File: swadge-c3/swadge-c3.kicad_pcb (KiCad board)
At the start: 2 copper layers, 73.7 x 89.4 mm, 73 parts, among them J1 USB_B_Micro, M1 Motor_DC, Q1 Q_NPN_BEC, SW0 4-1437565-2, SW1 4-1437565-2, SW2 4-1437565-2, SW3 4-1437565-2, SW4 LEVER8184, SW5 SW_SPDT, U1 GS321-TR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

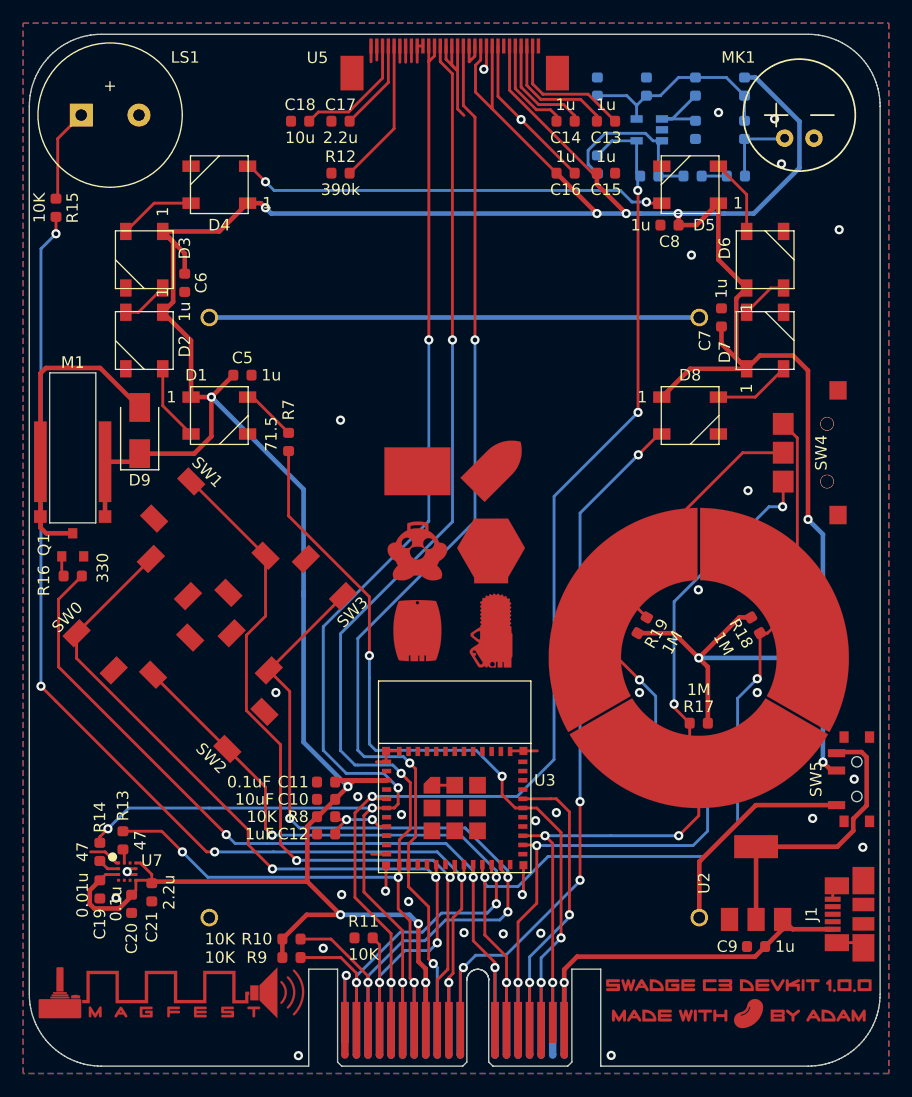
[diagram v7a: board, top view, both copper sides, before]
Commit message: Move around resistors, silk
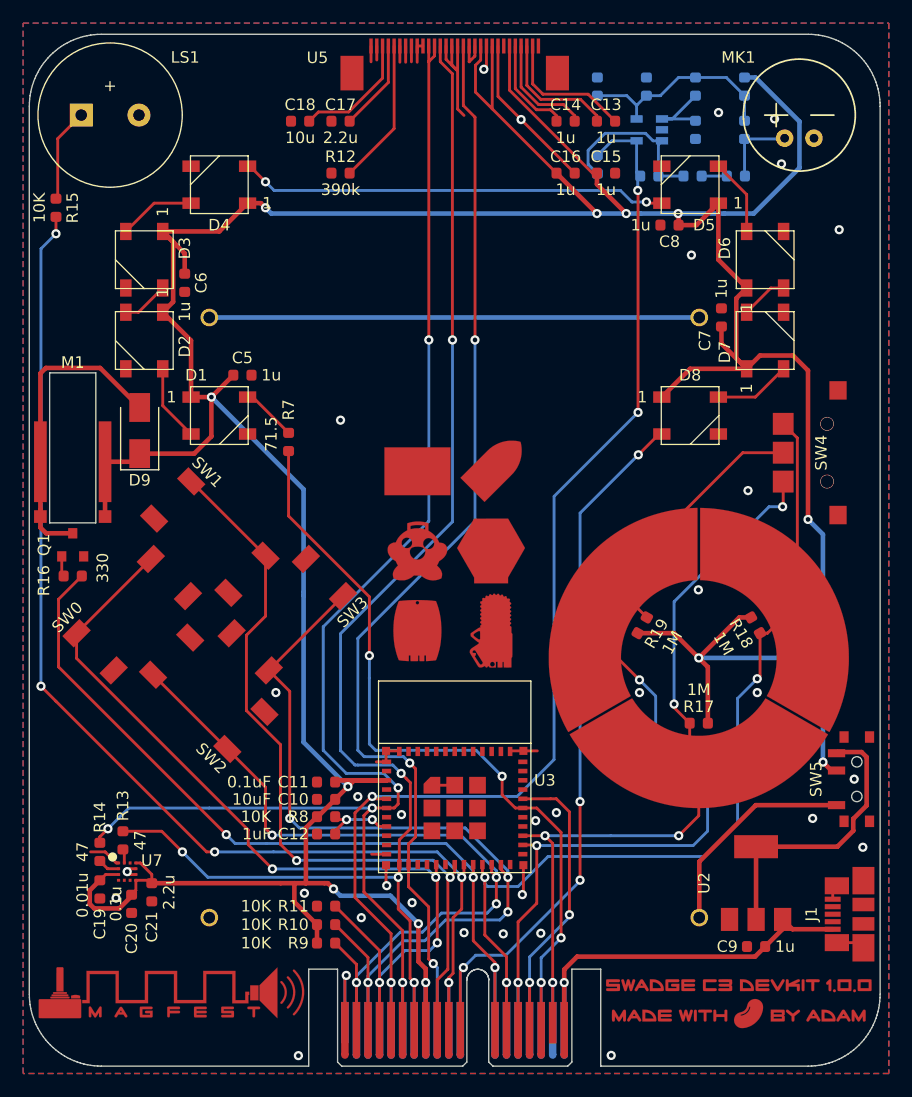
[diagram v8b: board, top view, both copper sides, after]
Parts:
- moved R11 4.26 mm to (134.2, 133.5)
- moved R10 3.25 mm to (134.2, 135.1)
- moved R9 3.25 mm to (134.2, 136.7)
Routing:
- net IO10_SW0: track 76.5 -> 80.6 mm
- net IO8_SW2: track 72.4 -> 70.3 mm
- net IO9_SW3: track 78.9 -> 77.4 mm
- net +3V3: track 379.6 -> 378.4 mm
